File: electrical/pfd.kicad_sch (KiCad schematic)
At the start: 12 parts

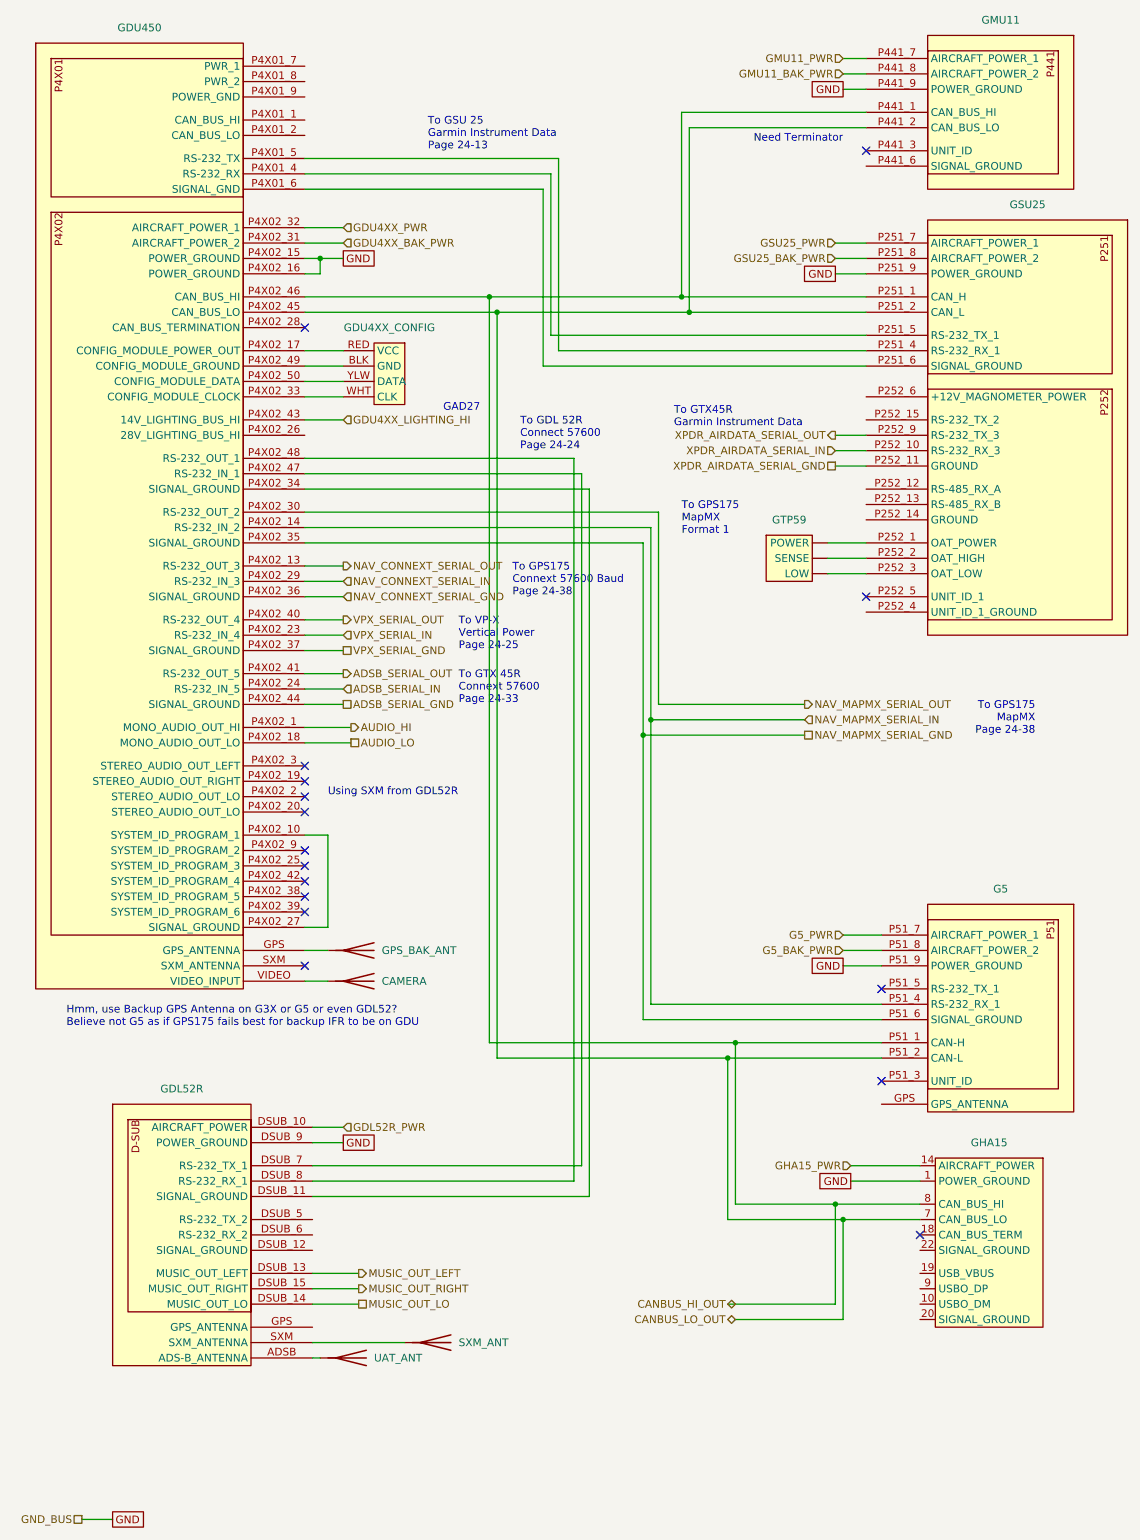
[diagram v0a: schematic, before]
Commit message: Changed grounds and canbuses to be in/out when applicable.
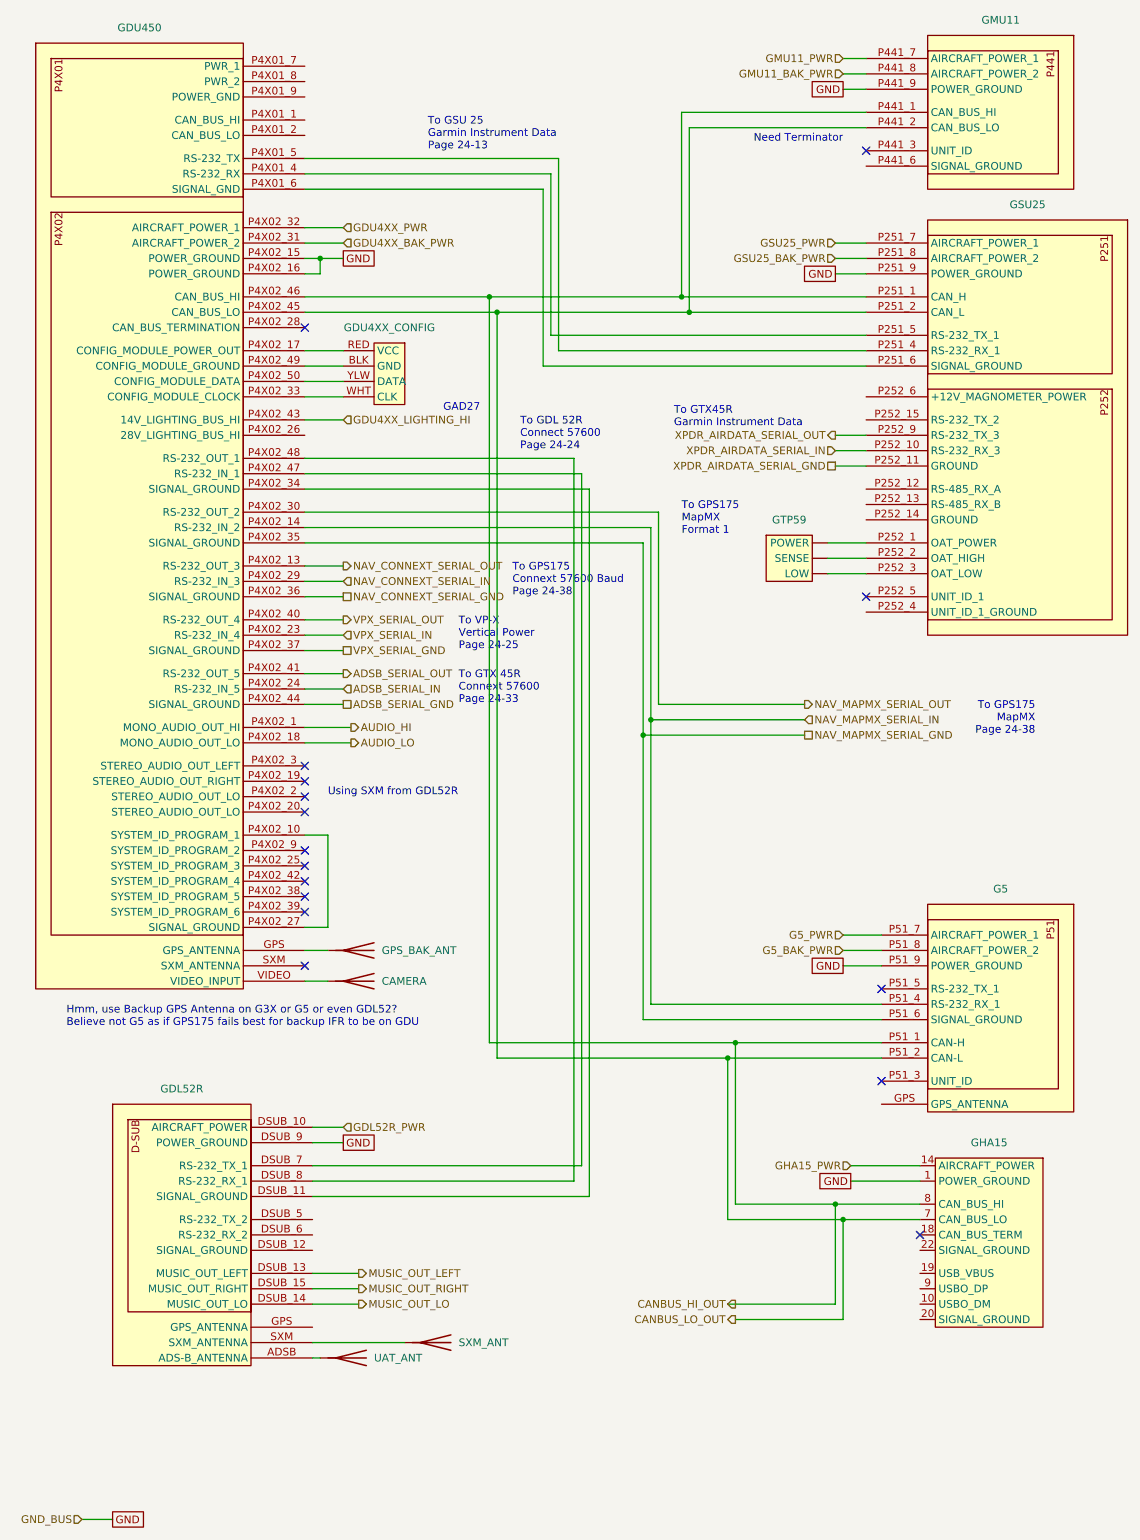
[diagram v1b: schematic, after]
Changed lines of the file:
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@@
     (effects (font (size 1.27 1.27)) (justify right))
   )
-  (hierarchical_label "MUSIC_OUT_LO" (shape passive) (at 71.12 226.06 0) (fields_autoplaced)
+  (hierarchical_label "MUSIC_OUT_LO" (shape output) (at 71.12 226.06 0) (fields_autoplaced)
     (effects (font (size 1.27 1.27)) (justify left))
   )
@@
     (effects (font (size 1.27 1.27)) (justify left))
   )
-  (hierarchical_label "CANBUS_HI_OUT" (shape bidirectional) (at 133.35 226.06 180) (fields_autoplaced)
+  (hierarchical_label "CANBUS_HI_OUT" (shape output) (at 133.35 226.06 180) (fields_autoplaced)
     (effects (font (size 1.27 1.27)) (justify right))
   )
@@
     (effects (font (size 1.27 1.27)) (justify left))
   )
-  (hierarchical_label "CANBUS_LO_OUT" (shape bidirectional) (at 133.35 228.6 180) (fields_autoplaced)
+  (hierarchical_label "CANBUS_LO_OUT" (shape output) (at 133.35 228.6 180) (fields_autoplaced)
     (effects (font (size 1.27 1.27)) (justify right))
   )
@@
     (effects (font (size 1.27 1.27)) (justify left))
   )
-  (hierarchical_label "GND_BUS" (shape passive) (at 25.4 261.62 180) (fields_autoplaced)
+  (hierarchical_label "GND_BUS" (shape input) (at 25.4 261.62 180) (fields_autoplaced)
     (effects (font (size 1.27 1.27)) (justify right))
   )
@@
     (effects (font (size 1.27 1.27)) (justify right))
   )
-  (hierarchical_label "NAV_CONNEXT_SERIAL_GND" (shape input) (at 68.58 109.22 0) (fields_autoplaced)
+  (hierarchical_label "NAV_CONNEXT_SERIAL_GND" (shape passive) (at 68.58 109.22 0) (fields_autoplaced)
     (effects (font (size 1.27 1.27)) (justify left))
   )
-  (hierarchical_label "AUDIO_LO" (shape passive) (at 69.85 133.35 0) (fields_autoplaced)
+  (hierarchical_label "AUDIO_LO" (shape output) (at 69.85 133.35 0) (fields_autoplaced)
     (effects (font (size 1.27 1.27)) (justify left))
   )

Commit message: Made minimal, and removed everything not needed. want to add GMC 507 back.
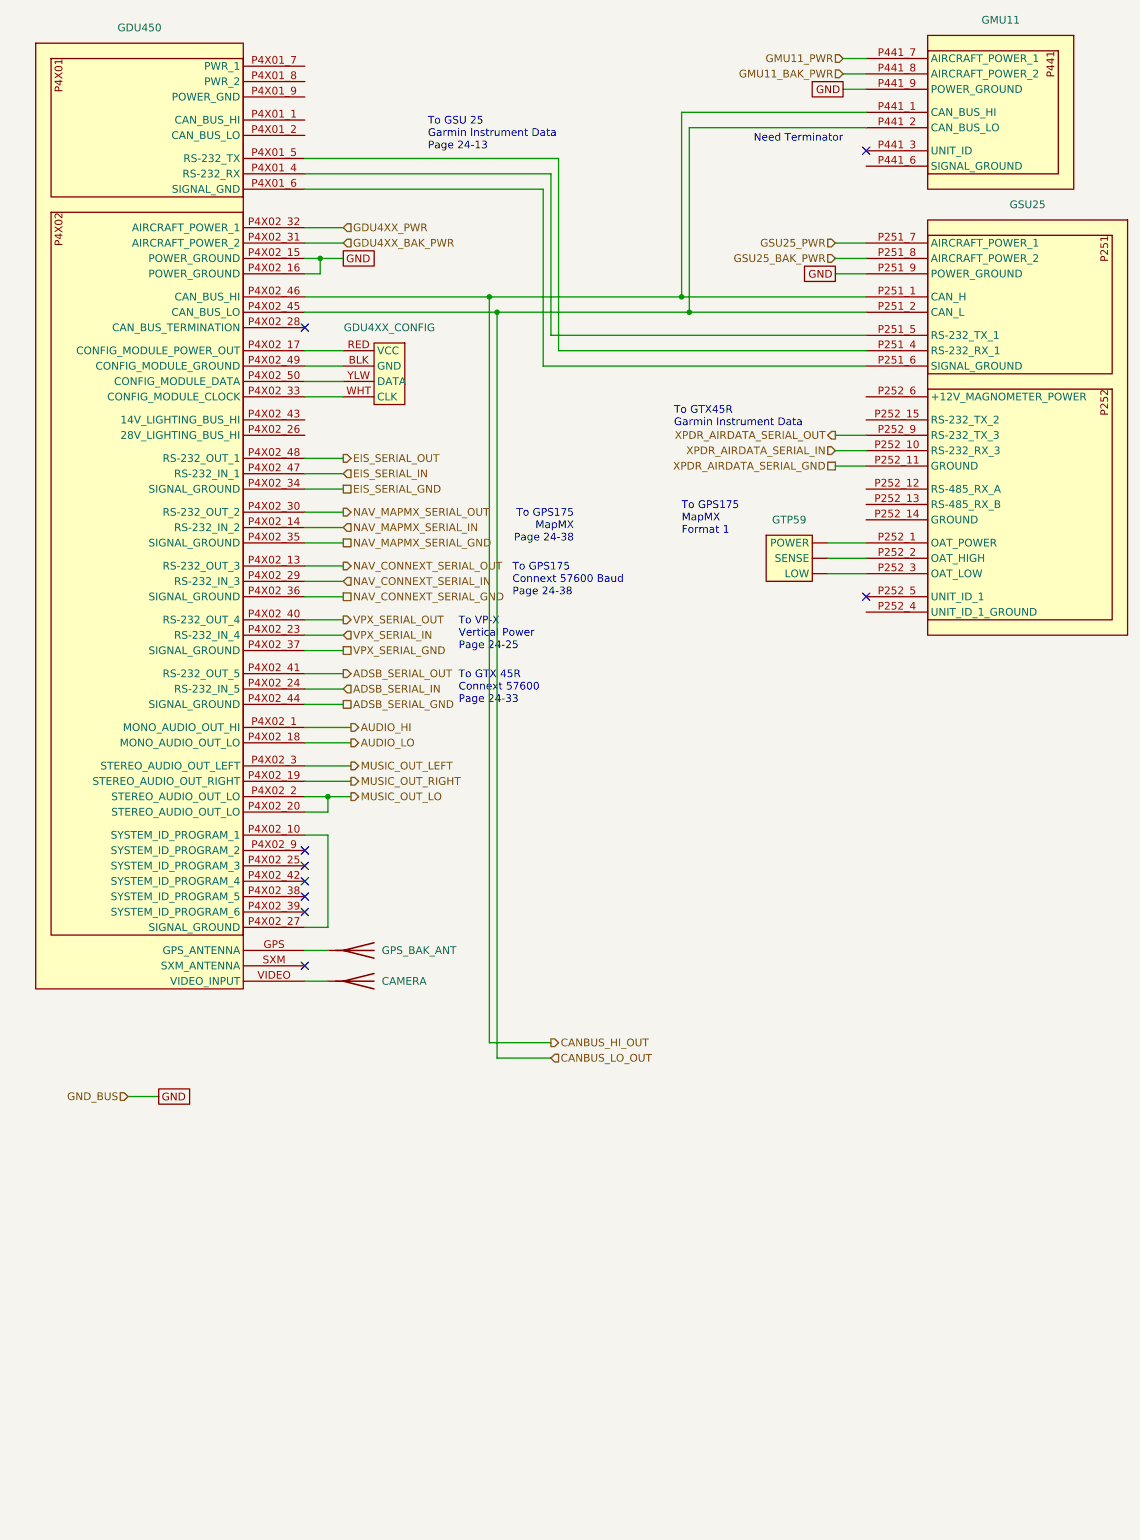
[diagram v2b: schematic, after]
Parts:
- removed G5: ~, symbol flyerx:Garmin_G5
- removed GDL52R: ~, symbol flyerx:Garmin_GDL52R
- removed GHA15: ~, symbol flyerx:Garmin_GHA15
- removed SXM_ANT, UAT_ANT: Antenna, symbol Device:Antenna
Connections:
- net MUSIC_OUT_LEFT: now also GDU450.P4X02_3 (STEREO_AUDIO_OUT_LEFT)
- net MUSIC_OUT_LO: now also GDU450.P4X02_2 (STEREO_AUDIO_OUT_LO), GDU450.P4X02_20 (STEREO_AUDIO_OUT_LO)
- net MUSIC_OUT_RIGHT: now also GDU450.P4X02_19 (STEREO_AUDIO_OUT_RIGHT)
- net EIS_SERIAL_GND: now reaches GDU450.P4X02_34 (SIGNAL_GROUND)
- net EIS_SERIAL_IN: now reaches GDU450.P4X02_47 (RS-232_IN_1)
- net EIS_SERIAL_OUT: now reaches GDU450.P4X02_48 (RS-232_OUT_1)
- net GDU4XX_LIGHTING_HI: no longer names the net of GDU450.P4X02_43 (14V_LIGHTING_BUS_HI)
- no-connect marks 16 -> 9
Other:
- note removed: "GAD27"
- note removed: "Hmm, use Backup GPS Antenna on G3X or G5 or even GDL52? Believe not G5 as if GPS175 fails best for backup IFR to be on GDU"
- note removed: "To GDL 52R Connect 57600 Page 24-24"
- note removed: "Using SXM from GDL52R"
